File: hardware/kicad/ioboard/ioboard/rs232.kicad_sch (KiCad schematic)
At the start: 0 parts

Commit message: Add RS232 schematic capture and wire it into the root sheet
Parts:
- added C24, C25, C26, C27, C29: 0.1uF, symbol Device:C
- added J6: Conn_01x03, symbol Connector_Generic:Conn_01x03
- added U16: MAX3232EIPWR, MAX3232EIPWR:SOP65P640X120-16N, symbol MAX3232EIPWR:MAX3232EIPWR
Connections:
- new net: C29.1, U16.2 (V+)
- new net: C24.1, U16.1 (C1+)
- new net: C24.2, U16.3 (C1-)
- new net: C25.1, U16.4 (C2+)
- new net: C25.2, U16.5 (C2-)
- new net: C27.1, U16.6 (V-)
- new net 3V3_LOGIC: C26.1, U16.16 (VCC)
- new net GND_LOGIC: C26.2, C27.2, C29.2, J6.3 (Pin_3), U16.15 (GND)
- new net RS232_RXD: U16.12 (ROUT1)
- new net RS232_TXD: U16.11 (DIN1)
- new net RXD: J6.2 (Pin_2), U16.13 (RIN1)
- new net TXD: J6.1 (Pin_1), U16.14 (DOUT1)
- no-connect marks 0 -> 4

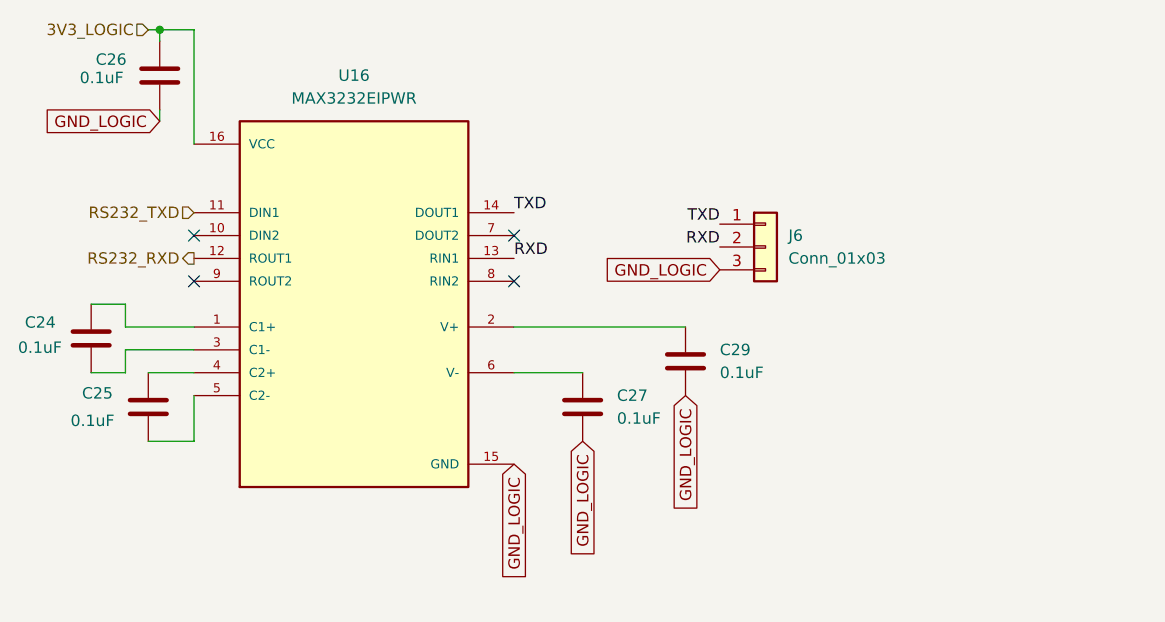
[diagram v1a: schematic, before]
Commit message: Close out RS232 subsystem; defer ERC to a single end-of-project pass
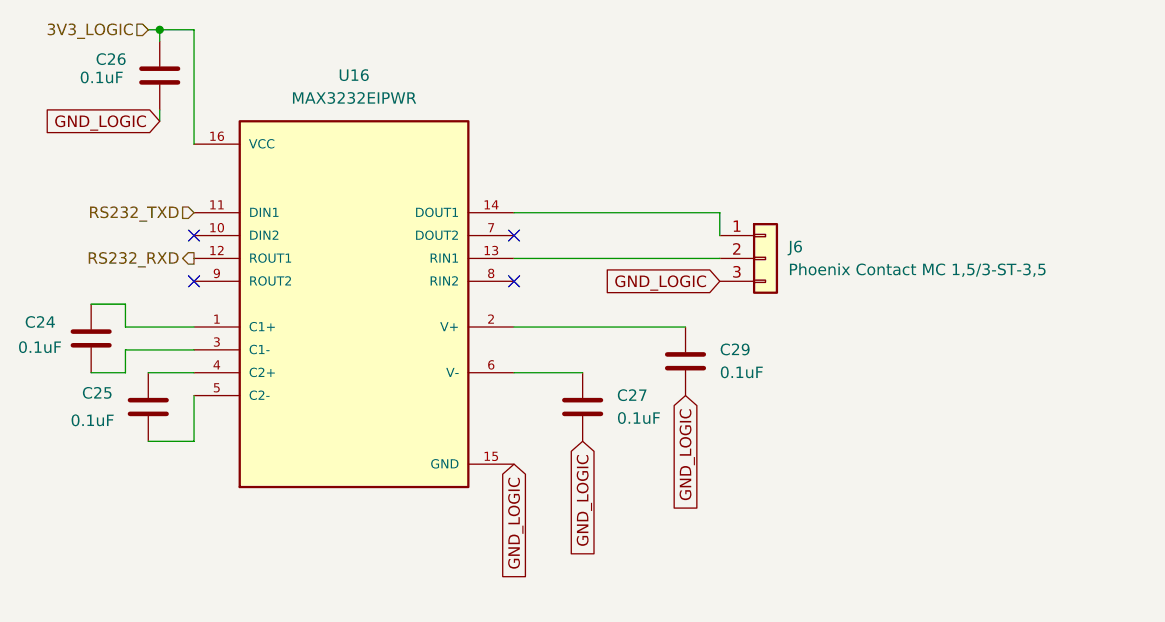
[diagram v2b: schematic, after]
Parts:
- J6: value Conn_01x03 -> Phoenix Contact MC 1,5/3-ST-3,5
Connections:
- net RXD: no longer names the net of J6.2 (Pin_2), U16.13 (RIN1)
- net TXD: no longer names the net of J6.1 (Pin_1), U16.14 (DOUT1)
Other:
- moved on the sheet: J6
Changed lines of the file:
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@@
+	(wire
+		(pts
+			(xy 139.7 67.31) (xy 139.7 69.85)
+		)
+		(stroke
+			(width 0)
+			(type default)
+		)
+	)
 	(wire
 		(pts
@@
 	(wire
 		(pts
+			(xy 116.84 72.39) (xy 139.7 72.39)
+		)
+		(stroke
+			(width 0)
+			(type default)
+		)
+	)
+	(wire
+		(pts
 			(xy 73.66 77.47) (xy 69.85 77.47)
 		)
@@
 	(wire
 		(pts
+			(xy 116.84 67.31) (xy 139.7 67.31)
+		)
+		(stroke
+			(width 0)
+			(type default)
+		)
+	)
+	(wire
+		(pts
 			(xy 77.47 48.26) (xy 77.47 46.99)
 		)
@@
 			(width 0)
 			(type default)
-		)
-	)
-	(label "TXD"
-		(at 116.84 67.31 0)
-		(effects
-			(font
-				(size 1.27 1.27)
-			)
-			(justify left bottom)
-		)
-	)
-	(label "RXD"
-		(at 116.84 72.39 0)
-		(effects
-			(font
-				(size 1.27 1.27)
-			)
-			(justify left bottom)
-		)
-	)
-	(label "TXD"
-		(at 139.7 68.58 180)
-		(effects
-			(font
-				(size 1.27 1.27)
-			)
-			(justify right bottom)
-		)
-	)
-	(label "RXD"
-		(at 139.7 71.12 180)
-		(effects
-			(font
-				(size 1.27 1.27)
-			)
-			(justify right bottom)
 		)
 	)
@@
 	(global_label "GND_LOGIC"
 		(shape input)
-		(at 139.7 73.66 180)
+		(at 139.7 74.93 180)
 		(fields_autoplaced yes)
 		(effects
@@
 		)
 		(property "Intersheetrefs" "${INTERSHEET_REFS}"
-			(at 126.3733 73.66 0)
+			(at 126.3733 74.93 0)
 			(effects
 				(font
@@
 	(symbol
 		(lib_id "Connector_Generic:Conn_01x03")
-		(at 144.78 71.12 0)
+		(at 144.78 72.39 0)
 		(unit 1)
 		(exclude_from_sim no)
@@
 		(fields_autoplaced yes)
 		(property "Reference" "J6"
-			(at 147.32 69.8499 0)
+			(at 147.32 71.1199 0)
 			(effects
 				(font
@@
 			)
 		)
-		(property "Value" "Conn_01x03"
-			(at 147.32 72.3899 0)
+		(property "Value" "Phoenix Contact MC 1,5/3-ST-3,5"
+			(at 147.32 73.6599 0)
 			(effects
 				(font
@@
 		)
 		(property "Footprint" ""
-			(at 144.78 71.12 0)
+			(at 144.78 72.39 0)
 			(effects
 				(font
@@
 		)
 		(property "Datasheet" "~"
-			(at 144.78 71.12 0)
+			(at 144.78 72.39 0)
 			(effects
 				(font
@@
 		)
 		(property "Description" "Generic connector, single row, 01x03, script generated (kicad-library-utils/schlib/autogen/connector/)"
-			(at 144.78 71.12 0)
-			(effects
-				(font
+			(at 144.78 72.39 0)
+			(effects
+				(font

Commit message: docs: add Ethernet (W5500) subsystem plan, lock front end/magnetics/LED design
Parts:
- renumbered C24 to C1, C25 to C2, C26 to C3, C27 to C4, C29 to C5, J6 to J1, U16 to U1
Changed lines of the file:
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@@
 		(dnp no)
 		(fields_autoplaced yes)
-		(property "Reference" "C29"
+		(property "Reference" "C5"
 			(at 139.7 82.5499 0)
 			(effects
@@
 				(path "/a0fa9f92-ef51-408b-9617-1545f9e9dad8/76e19aa2-12ff-4bfe-8bd8-7b7c95f6f393"
 					(reference "C29")
+					(unit 1)
+				)
+			)
+			(project "rs232"
+				(path "/a76a627e-24a2-4a76-844a-c9490240f8fe"
+					(reference "C5")
 					(unit 1)
 				)
@@
 		(dnp no)
 		(fields_autoplaced yes)
-		(property "Reference" "U16"
+		(property "Reference" "U1"
 			(at 99.06 52.07 0)
 			(effects
@@
 				(path "/a0fa9f92-ef51-408b-9617-1545f9e9dad8/76e19aa2-12ff-4bfe-8bd8-7b7c95f6f393"
 					(reference "U16")
+					(unit 1)
+				)
+			)
+			(project "rs232"
+				(path "/a76a627e-24a2-4a76-844a-c9490240f8fe"
+					(reference "U1")
 					(unit 1)
 				)
@@
 		(dnp no)
 		(fields_autoplaced yes)
-		(property "Reference" "J6"
+		(property "Reference" "J1"
 			(at 147.32 71.1199 0)
 			(effects
@@
 				(path "/a0fa9f92-ef51-408b-9617-1545f9e9dad8/76e19aa2-12ff-4bfe-8bd8-7b7c95f6f393"
 					(reference "J6")
+					(unit 1)
+				)
+			)
+			(project "rs232"
+				(path "/a76a627e-24a2-4a76-844a-c9490240f8fe"
+					(reference "J1")
 					(unit 1)
 				)
@@
 		(on_board yes)
 		(dnp no)
-		(property "Reference" "C24"
+		(property "Reference" "C1"
 			(at 62.484 79.502 0)
 			(effects
@@
 				(path "/a0fa9f92-ef51-408b-9617-1545f9e9dad8/76e19aa2-12ff-4bfe-8bd8-7b7c95f6f393"
 					(reference "C24")
+					(unit 1)
+				)
+			)
+			(project "rs232"
+				(path "/a76a627e-24a2-4a76-844a-c9490240f8fe"
+					(reference "C1")
 					(unit 1)
 				)
@@
 		(on_board yes)
 		(dnp no)
-		(property "Reference" "C25"
+		(property "Reference" "C2"
 			(at 68.834 87.376 0)
 			(effects
@@
 				(path "/a0fa9f92-ef51-408b-9617-1545f9e9dad8/76e19aa2-12ff-4bfe-8bd8-7b7c95f6f393"
 					(reference "C25")
+					(unit 1)
+				)
+			)
+			(project "rs232"
+				(path "/a76a627e-24a2-4a76-844a-c9490240f8fe"
+					(reference "C2")
 					(unit 1)
 				)
@@
 		(on_board yes)
 		(dnp no)
-		(property "Reference" "C26"
+		(property "Reference" "C3"
 			(at 70.358 50.292 0)
 			(effects
@@
 				(path "/a0fa9f92-ef51-408b-9617-1545f9e9dad8/76e19aa2-12ff-4bfe-8bd8-7b7c95f6f393"
 					(reference "C26")
+					(unit 1)
+				)
+			)
+			(project "rs232"
+				(path "/a76a627e-24a2-4a76-844a-c9490240f8fe"
+					(reference "C3")
 					(unit 1)
 				)
@@
 		(dnp no)
 		(fields_autoplaced yes)
-		(property "Reference" "C27"
+		(property "Reference" "C4"
 			(at 128.27 87.6299 0)
 			(effects
@@
 				)
 			)
-		)
-	)
+			(project "rs232"
+				(path "/a76a627e-24a2-4a76-844a-c9490240f8fe"
+					(reference "C4")
+					(unit 1)
+				)
+			)
+		)
+	)
+	(sheet_instances
+		(path "/"
+			(page "1")
+		)
+	)
+	(embedded_fonts no)
 )
